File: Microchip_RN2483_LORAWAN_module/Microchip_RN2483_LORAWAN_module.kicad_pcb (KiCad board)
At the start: 2 copper layers, 9 parts, among them P1 SMA_mini, U1 RN2483, U2 wireless_patice

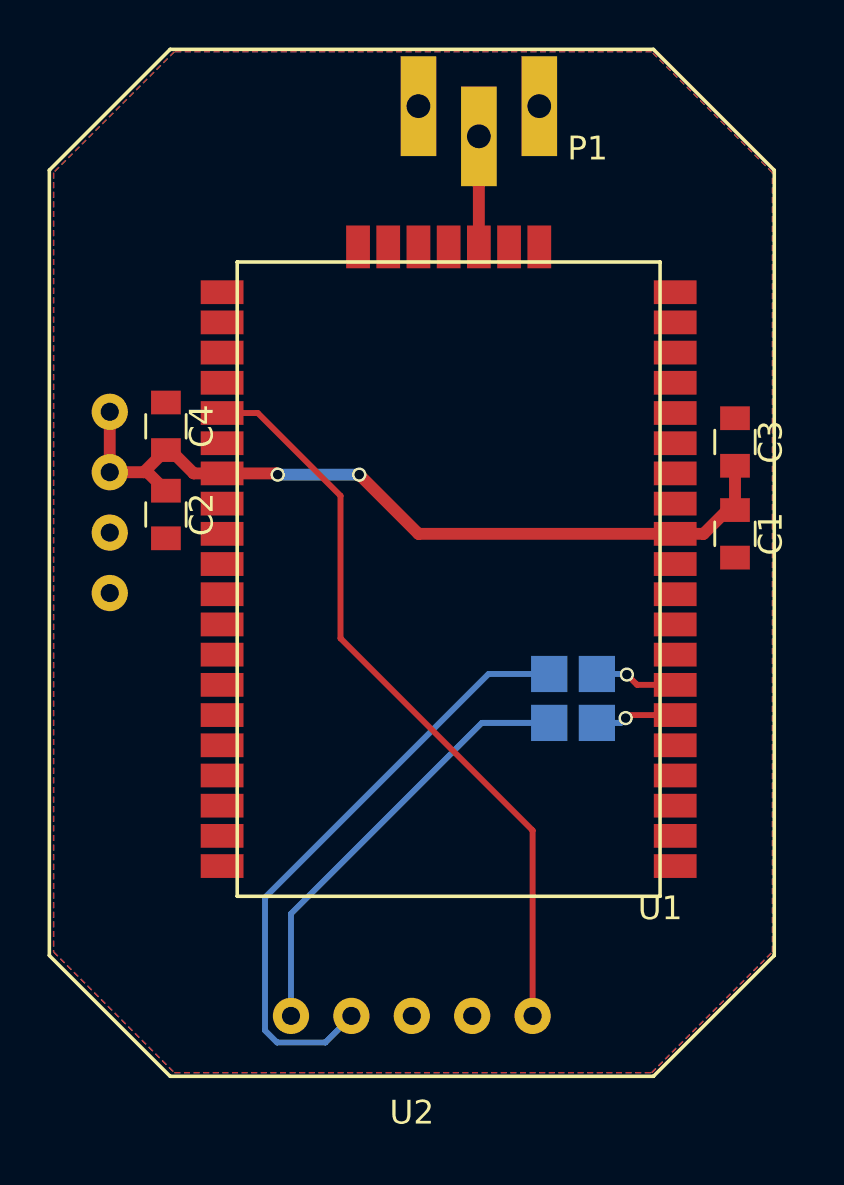
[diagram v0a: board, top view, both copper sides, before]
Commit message: objednavka snpm a microchip redukce
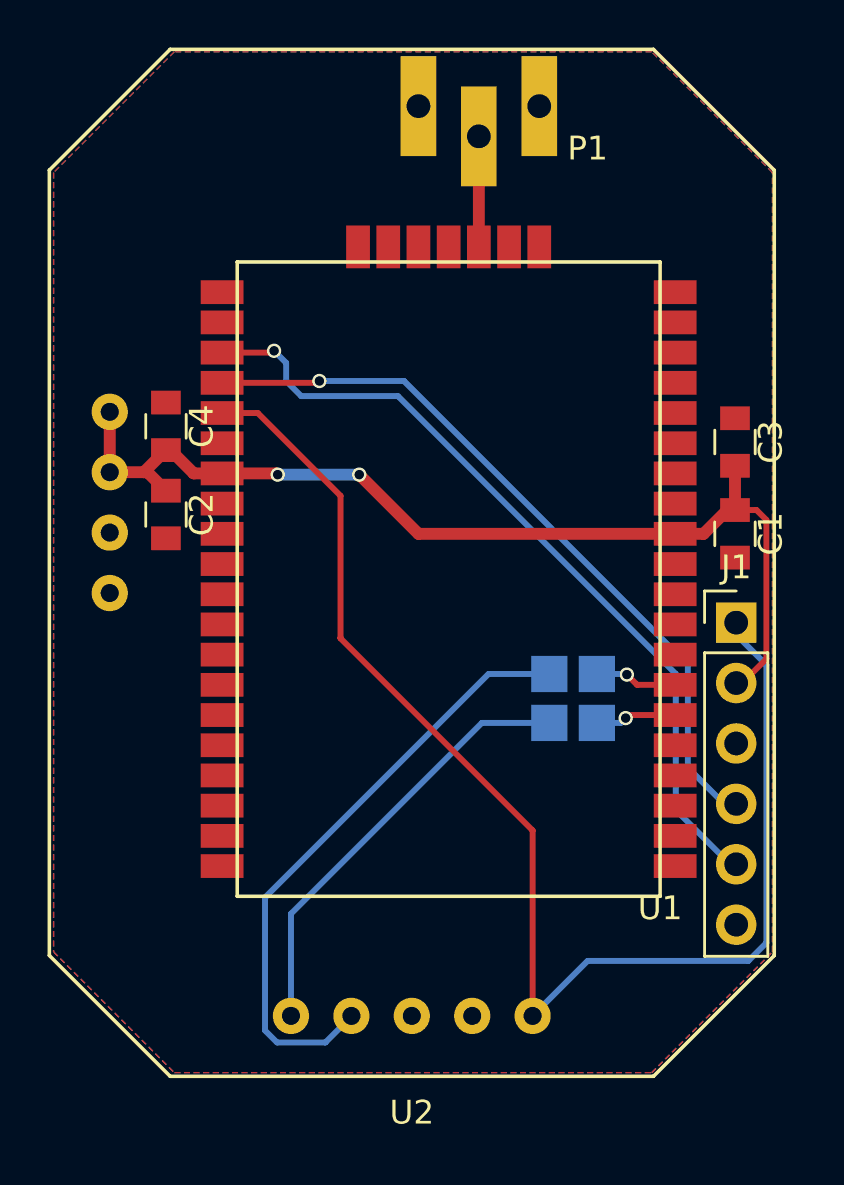
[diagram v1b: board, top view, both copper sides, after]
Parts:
- added J1: Conn_01x06, lorawan_module:Pin_Header_Straight_1x06_Pitch2.54mm, F.Cu at (158.2, 101.2)
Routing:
- net Net-(J1-Pad5): track 0.00 -> 34.4 mm, vias 0 -> 1
- net Net-(J1-Pad4): track 0.00 -> 31.5 mm, vias 0 -> 1
- net rn2483_reset: track 31.6 -> 56.7 mm
- net +3V3: track 35.0 -> 44.2 mm
